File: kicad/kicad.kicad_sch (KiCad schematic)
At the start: 240 parts, among them Q0 MNMOS, Q1 MNMOS, Q10 MNMOS, Q100 MNMOS, Q101 MNMOS, Q102 MNMOS, Q103 MNMOS, Q104 MNMOS, Q105 MNMOS, Q106 MNMOS, Q107 MNMOS, Q108 MNMOS, Q109 MNMOS, Q11 MNMOS, Q110 MNMOS, Q111 MNMOS, Q112 MNMOS, Q113 MNMOS, Q114 MNMOS, Q115 MNMOS, Q116 MNMOS, Q117 MNMOS, Q118 MNMOS, Q119 MNMOS, Q12 MNMOS, Q120 MNMOS, Q121 MNMOS, Q122 MNMOS, Q123 MNMOS, Q124 MNMOS, Q125 MNMOS, Q127 MNMOS, Q128 MNMOS, Q129 MNMOS, Q13 MNMOS, Q130 MNMOS, Q14 MNMOS, Q15 MNMOS, Q16 MNMOS, Q17 MNMOS, Q18 MNMOS, Q19 MNMOS, Q2 MNMOS, Q20 MNMOS, Q21 MNMOS, Q22 MNMOS, Q23 MNMOS, Q24 MNMOS, Q25 MNMOS, Q26 MNMOS, Q27 MNMOS, Q28 MNMOS, Q29 MNMOS, Q3 MNMOS, Q30 MNMOS, Q31 MNMOS, Q32 MNMOS, Q33 MNMOS, Q34 MNMOS, Q35 MNMOS, Q36 MNMOS, Q37 MNMOS, Q38 MNMOS, Q39 MNMOS, Q4 MNMOS, Q40 MNMOS, Q41 MNMOS, Q42 MNMOS, Q43 MNMOS, Q44 MNMOS, Q45 MNMOS, Q46 MNMOS, Q47 MNMOS, Q48 MNMOS, Q49 MNMOS, Q5 MNMOS, Q50 MNMOS, Q51 MNMOS, Q52 MNMOS, Q53 MNMOS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

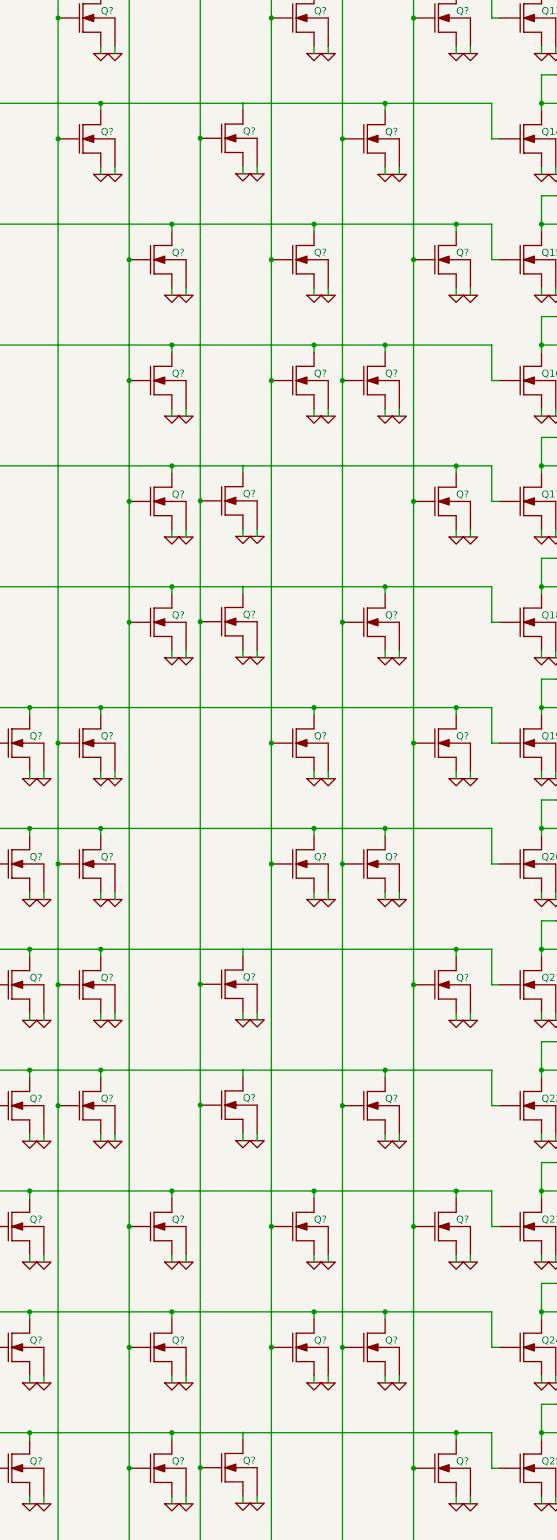
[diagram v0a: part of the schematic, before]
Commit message: Region 1 finished
Signed-off-by: Joppe Blondel <joppe@blondel.nl>
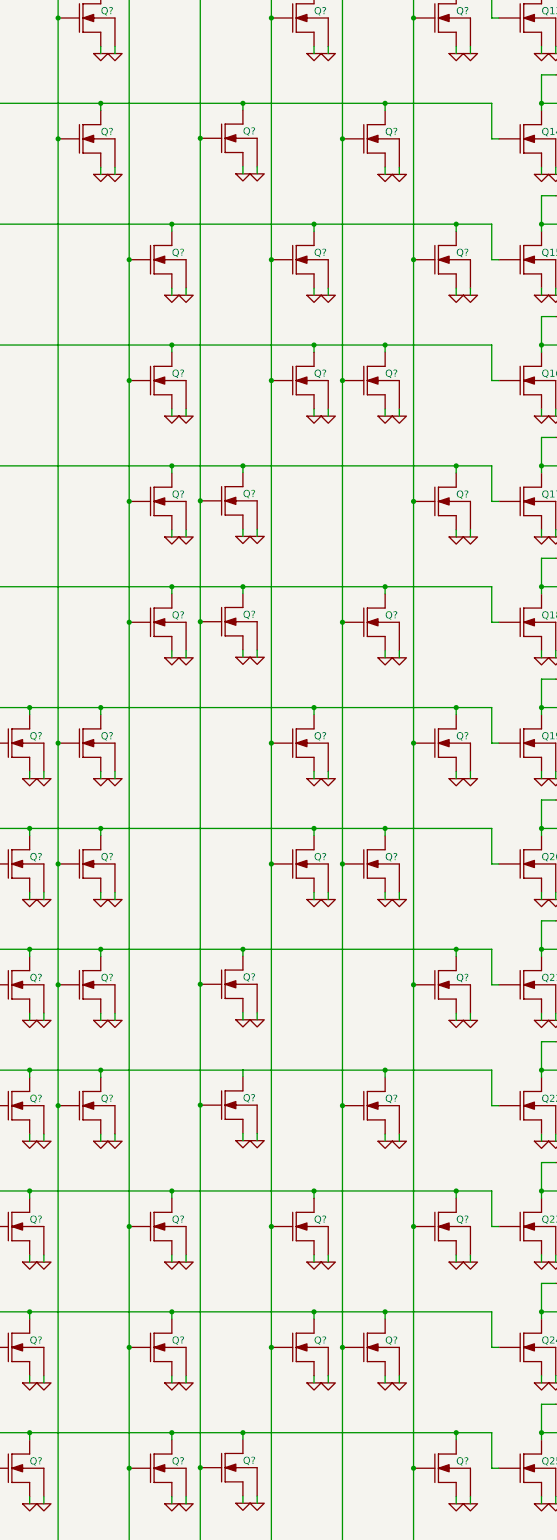
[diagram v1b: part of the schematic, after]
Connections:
- net at Q17.2 (G), Q?.1 (D), Q?.1 (D)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: now also Q?.1 (D)
- net at Q21.2 (G), Q?.1 (D), Q?.1 (D)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: now also Q?.1 (D)
- net at Q25.2 (G), Q?.1 (D), Q?.1 (D)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: now also Q?.1 (D)
- net at Q14.2 (G), Q?.1 (D), Q?.1 (D)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: now also Q?.1 (D)
- net at Q?.1 (D): now also Q18.2 (G), Q?.1 (D), Q?.1 (D), Q?.1 (D), R18.2
